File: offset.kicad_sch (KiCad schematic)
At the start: 37 parts, among them U11 OPA2189DGK, U12 TMUX1108PW, U18 DG419D, U19 TCA0372

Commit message: Tweaks following spice simulation.
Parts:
- removed R120, R121: 0R33, Resistor_SMD:R_0805_2012Metric, symbol Device:R
- C101, C102: value 1u -> 10n; footprint Capacitor_SMD:C_0402_1005Metric -> Capacitor_SMD:C_0603_1608Metric; LCSC C52923 -> C307500
- C104, C116: value 0u1 -> 1u; LCSC C307331 -> C52923
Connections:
- net at C110.1, C112.1, U19.1 (VCC): now also L11.2
- net at L12.2: now also C111.2, C113.2, U19.12 (VEE), U19.13 (VEE), U19.4 (VEE), U19.5 (VEE)
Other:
- moved on the sheet: C110, C111, C112, C113, C116, L11, L12, U18, U19C

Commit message: About to delete scan...
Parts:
- R114, R116: Stock (none) -> 50
- U11: Stock (none) -> 15
- U12, U19: Stock (none) -> 3
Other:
- note added: "FIXME - can drive capacitance via mux?"

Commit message: Scan deleted.
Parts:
- removed C110, C111: 10u, Capacitor_SMD:C_0805_2012Metric, symbol Device:C
- removed C112, C113, C114, C115: 0u1, Capacitor_SMD:C_0402_1005Metric, symbol Device:C
- removed C116: 1u, Capacitor_SMD:C_0402_1005Metric, symbol Device:C
- removed L11, L12: 100, Inductor_SMD:L_0603_1608Metric, symbol Parts:L_Ferrite_Power
- removed U18: DG419D, Package_SO:SOIC-8_3.9x4.9mm_P1.27mm, symbol Parts:DG419
- removed U19: TCA0372, Package_SO:SOIC-16W_7.5x10.3mm_P1.27mm, symbol Parts:TCA0372

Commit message: Most blocks there....
About to restore scan.
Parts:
- added R119: 100, Resistor_SMD:R_0402_1005Metric, symbol Device:R
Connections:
- net 5V: now also R119.2; no longer R101.1, U11.1, U11.2 (-)
- new net: R101.1, R119.1, U11.1, U11.2 (-)
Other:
- note removed: "FIXME - can drive capacitance via mux?"
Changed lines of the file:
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@@
 		(title "Offset Voltage Generation")
 	)
-	(text "FIXME - can drive capacitance via mux?\n"
-		(exclude_from_sim no)
-		(at 143.256 56.134 0)
-		(effects
-			(font
-				(size 1.27 1.27)
-			)
-		)
-	)
 	(text_box "Tie the ladder grounds together with the compensation resistances to cancel currents."
 		(exclude_from_sim no)
@@
 	(wire
 		(pts
-			(xy 123.19 59.69) (xy 143.51 59.69)
+			(xy 123.19 59.69) (xy 124.46 59.69)
 		)
 		(stroke
@@
 	(wire
 		(pts
+			(xy 132.08 59.69) (xy 143.51 59.69)
+		)
+		(stroke
+			(width 0)
+			(type default)
+		)
+	)
+	(wire
+		(pts
 			(xy 95.25 57.15) (xy 100.33 57.15)
 		)
@@
 		(dnp no)
 		(property "Reference" "R101"
-			(at 130.81 61.214 90)
+			(at 125.73 63.246 90)
 			(effects
 				(font
 					(size 1.27 1.27)
 				)
-				(justify right)
+				(justify left)
 			)
 		)
@@
 		(dnp no)
 		(property "Reference" "R102"
-			(at 125.476 65.024 90)
+			(at 130.81 67.056 90)
 			(effects
 				(font
 					(size 1.27 1.27)
 				)
-				(justify left)
+				(justify right)
 			)
 		)
@@
 					(unit 1)
 				)
+			)
+		)
+	)
+	(symbol
+		(lib_id "Device:R")
+		(at 128.27 59.69 90)
+		(unit 1)
+		(exclude_from_sim no)
+		(in_bom yes)
+		(on_board yes)
+		(dnp no)
+		(property "Reference" "R119"
+			(at 128.27 57.658 90)
+			(effects
+				(font
+					(size 1.27 1.27)
+				)
+			)
+		)
+		(property "Value" "100"
+			(at 128.27 59.69 90)
+			(effects
+				(font
+					(size 1.27 1.27)
+				)
+			)
+		)
+		(property "Footprint" "Resistor_SMD:R_0402_1005Metric"
+			(at 128.27 61.468 90)
+			(effects
+				(font
+					(size 1.27 1.27)
+				)
+				(hide yes)
+			)
+		)
+		(property "Datasheet" "~"
+			(at 128.27 59.69 0)
+			(effects
+				(font
+					(size 1.27 1.27)
+				)
+				(hide yes)
+			)
+		)
+		(property "Description" "Resistor"
+			(at 128.27 59.69 0)
+			(effects
+				(font
+					(size 1.27 1.27)
+				)
+				(hide yes)
+			)
+		)
+		(property "LCSC" "C25076"
+			(at 128.27 59.69 90)
+			(effects
+				(font
+					(size 1.27 1.27)
+				)
+				(hide yes)
+			)
+		)
+		(property "Stock" ""
+			(at 128.27 59.69 90)
+			(effects
+				(font
+					(size 1.27 1.27)
+				)
+				(hide yes)
+			)
+		)
+		(pin "1"
+		)
+		(pin "2"
+		)
+		(instances
+			(project "lincal"
+				(path "/b054cef4-39e3-49d8-aff0-7ba5a206c187/fd210975-34eb-456f-9075-cf344b0a559b"
+					(reference "R119")
+					(unit 1)
+				)

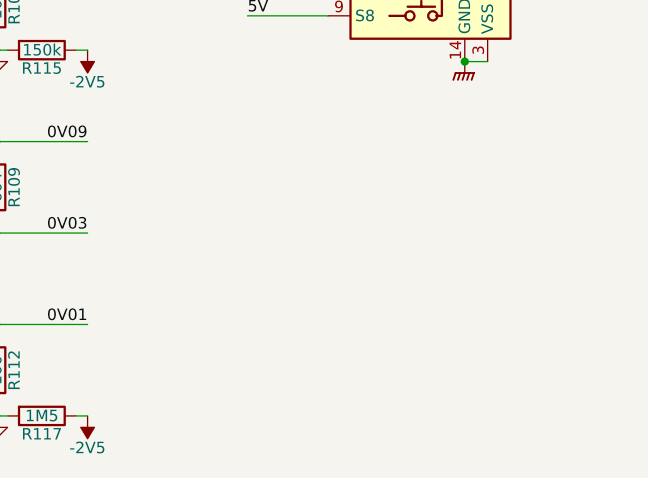
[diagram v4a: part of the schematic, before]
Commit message: S&H restored.  Now to touch up connections etc.
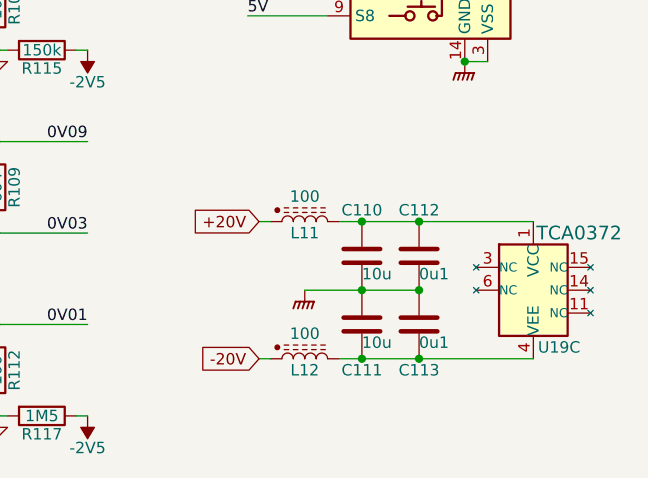
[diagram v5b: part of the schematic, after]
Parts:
- added C110, C111: 10u, Capacitor_SMD:C_0805_2012Metric, symbol Device:C
- added C112, C113: 0u1, Capacitor_SMD:C_0402_1005Metric, symbol Device:C
- added L11, L12: 100, Inductor_SMD:L_0603_1608Metric, symbol Parts:L_Ferrite_Power
- added U19: TCA0372, Package_SO:SOIC-16W_7.5x10.3mm_P1.27mm, symbol Parts:TCA0372
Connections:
- net GNDPWR: now also C110.2, C111.1, C112.2, C113.1
- new net: C110.1, C112.1, L11.2, U19.1 (VCC)
- new net: C111.2, C113.2, L12.2, U19.12 (VEE), U19.13 (VEE), U19.4 (VEE), U19.5 (VEE)
- new net +20V: L11.1
- new net -20V: L12.1

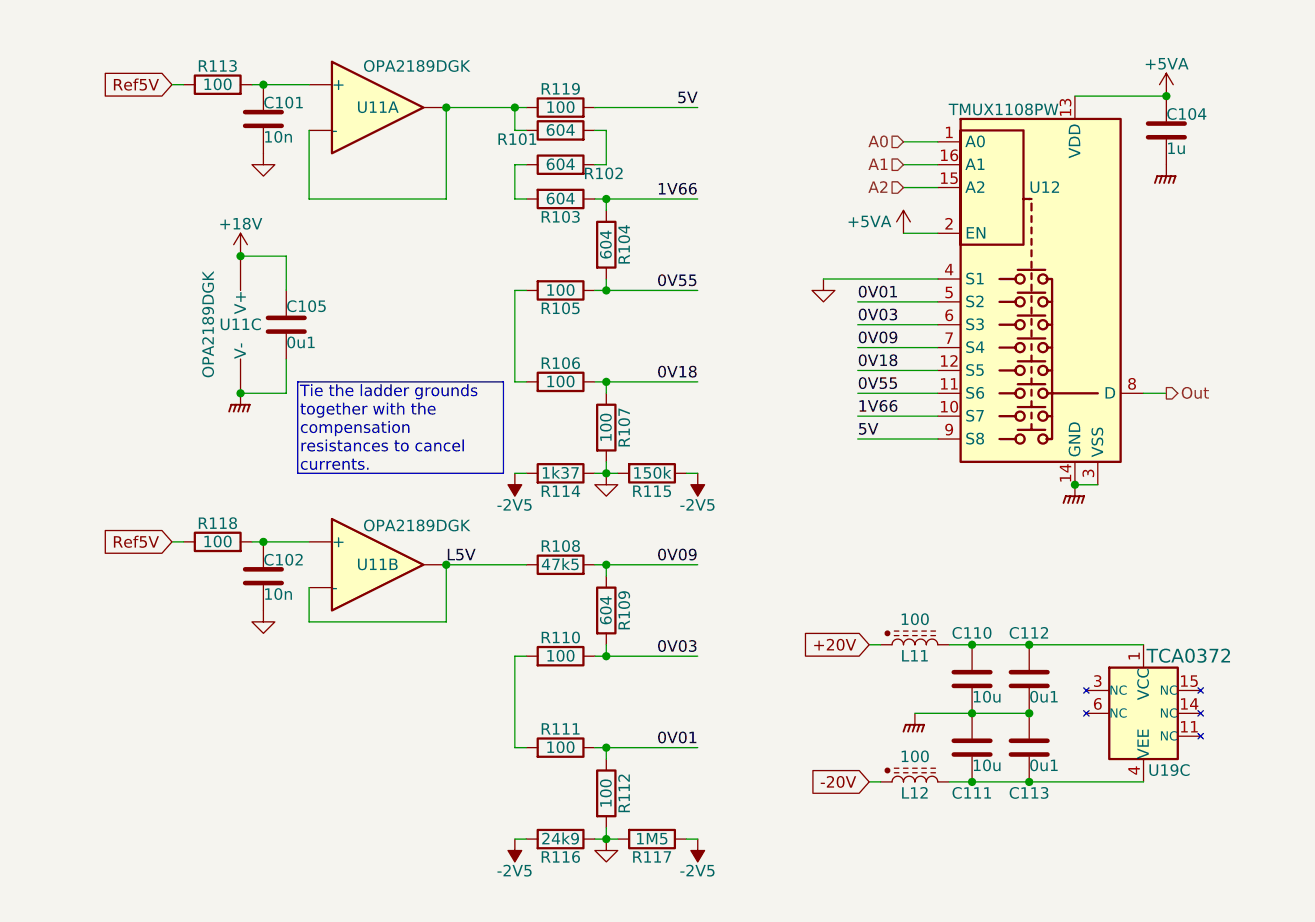
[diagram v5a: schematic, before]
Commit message: Put ref filtering into the schematic.
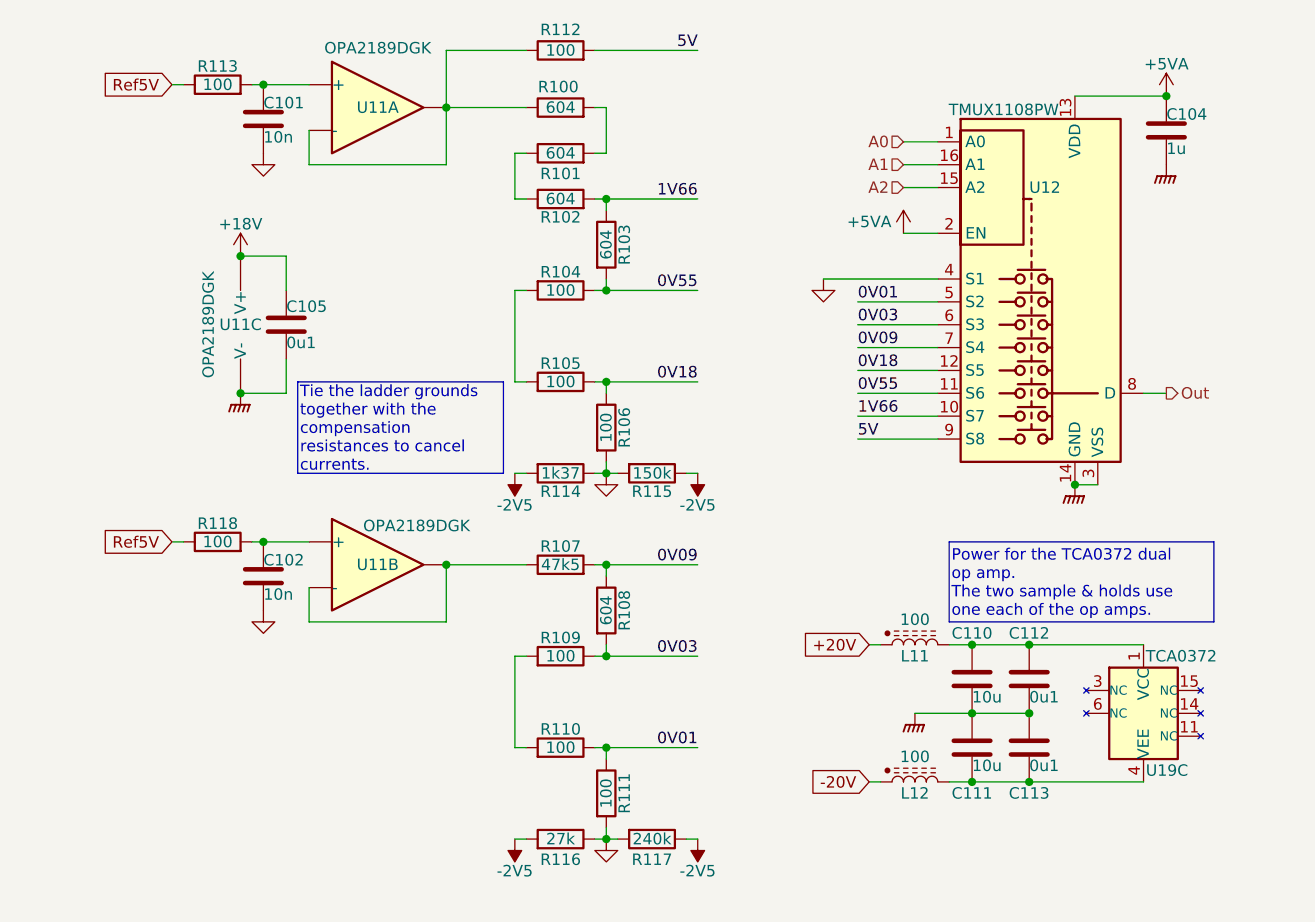
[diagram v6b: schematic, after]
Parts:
- removed R103: 604, Resistor_SMD:R_0603_1608Metric, symbol Device:R
- removed R119: 100, Resistor_SMD:R_0402_1005Metric, symbol Device:R
- added R100: 604, Resistor_SMD:R_0805_2012Metric, symbol Device:R
- added R112: 100, Resistor_SMD:R_0402_1005Metric, symbol Device:R
- R101, R102: footprint Resistor_SMD:R_0603_1608Metric -> Resistor_SMD:R_0805_2012Metric
- R114: footprint Resistor_SMD:R_0603_1608Metric -> (none); Stock 50 -> (none)
- R116: value 24k9 -> 27k; Stock 50 -> (none); now in the parts list
- R117: value 1M5 -> 240k; LCSC C4172 -> (none)
- renumbered R104 to R103, R105 to R104, R106 to R105, R107 to R106, R108 to R107, R109 to R108, R110 to R109, R111 to R110, R112 to R111
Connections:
- net 1V66: now also R102.2
- net 5V: now also R112.2
- net at U11.1, U11.2 (-): now also R100.1, R112.1; no longer R101.1
- net at R101.2: now also R100.2; no longer R102.2
- net at R102.1: now also R101.1
- net L5V: no longer names the net of R107.1, U11.6 (-), U11.7
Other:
- moved on the sheet: R101, R102

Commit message: Adjust voltage rails.
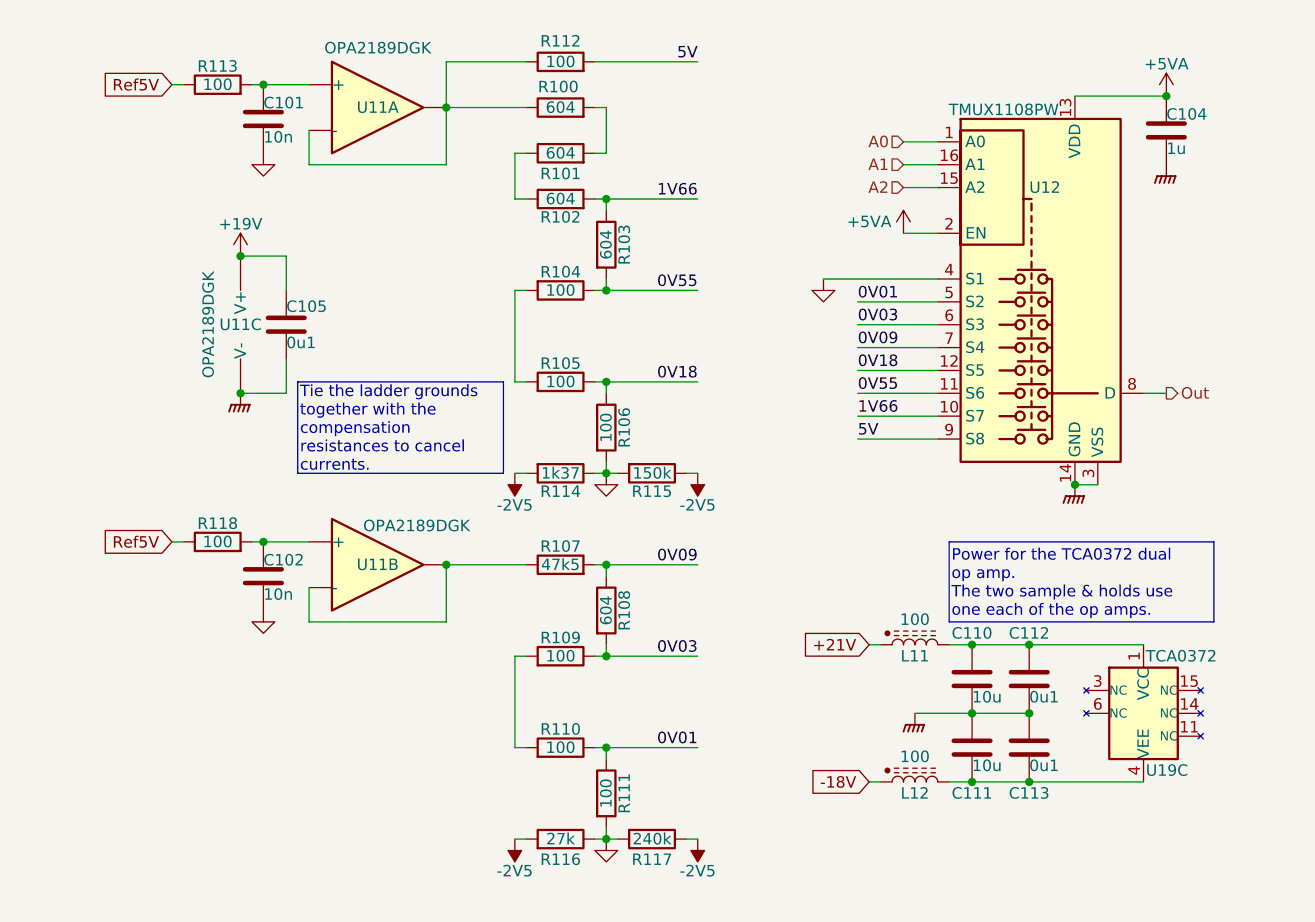
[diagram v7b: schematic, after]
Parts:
- R100, R101, R102: footprint Resistor_SMD:R_0805_2012Metric -> Resistor_SMD:R_0603_1608Metric
- R114: footprint (none) -> Resistor_SMD:R_0603_1608Metric; Stock (none) -> 50
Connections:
- net +18V renamed +19V
- net +20V renamed +21V
- net -20V renamed -18V
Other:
- moved on the sheet: R112
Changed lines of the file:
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@@
 	(wire
 		(pts
-			(xy 124.46 53.34) (xy 115.57 53.34)
+			(xy 124.46 54.61) (xy 115.57 54.61)
 		)
 		(stroke
@@
 	(wire
 		(pts
-			(xy 132.08 53.34) (xy 143.51 53.34)
+			(xy 132.08 54.61) (xy 143.51 54.61)
 		)
 		(stroke
@@
 	(wire
 		(pts
-			(xy 115.57 53.34) (xy 115.57 59.69)
+			(xy 115.57 54.61) (xy 115.57 59.69)
 		)
 		(stroke
@@
 	)
 	(label "5V"
-		(at 143.51 53.34 180)
+		(at 143.51 54.61 180)
 		(effects
 			(font
@@
 		)
 	)
-	(global_label "+20V"
+	(global_label "+21V"
 		(shape input)
 		(at 162.56 119.38 180)
@@
 		)
 	)
-	(global_label "-20V"
+	(global_label "-18V"
 		(shape input)
 		(at 162.56 134.62 180)
@@
 			)
 		)
-		(property "Footprint" "Resistor_SMD:R_0805_2012Metric"
+		(property "Footprint" "Resistor_SMD:R_0603_1608Metric"
 			(at 128.27 66.548 90)
 			(effects
@@
 	)
 	(symbol
-		(lib_id "Parts:+18V")
+		(lib_id "Parts:+19V")
 		(at 92.71 76.2 0)
 		(mirror y)
@@
 		(on_board yes)
 		(dnp no)
-		(property "Reference" "#PWR0117"
+		(property "Reference" "#PWR117"
 			(at 92.71 80.01 0)
 			(effects
@@
 			)
 		)
-		(property "Value" "+18V"
+		(property "Value" "+19V"
 			(at 92.71 72.644 0)
 			(do_not_autoplace yes)
@@
 			)
 		)
-		(property "Description" "Power symbol creates a global label with name {dblquote}+18V{dblquote}"
+		(property "Description" "Power symbol creates a global label with name \"+19\""
 			(at 92.71 76.2 0)
 			(effects
@@
 			(project ""
 				(path "/b054cef4-39e3-49d8-aff0-7ba5a206c187/fd210975-34eb-456f-9075-cf344b0a559b"
-					(reference "#PWR0117")
+					(reference "#PWR117")
 					(unit 1)
 				)
@@
 	(symbol
 		(lib_id "Device:R")
-		(at 128.27 53.34 90)
+		(at 128.27 54.61 90)
 		(unit 1)
 		(exclude_from_sim no)
@@
 		(dnp no)
 		(property "Reference" "R112"
-			(at 128.27 51.054 90)
+			(at 128.27 52.324 90)
 			(effects
 				(font
@@
 		)
 		(property "Value" "100"
-			(at 128.27 53.34 90)
+			(at 128.27 54.61 90)
 			(effects
 				(font
@@
 		)
 		(property "Footprint" "Resistor_SMD:R_0402_1005Metric"
-			(at 128.27 55.118 90)
+			(at 128.27 56.388 90)
 			(effects
 				(font
@@
 		)
 		(property "Datasheet" "~"
-			(at 128.27 53.34 0)
+			(at 128.27 54.61 0)
 			(effects
 				(font
@@
 		)
 		(property "Description" "Resistor"
-			(at 128.27 53.34 0)
+			(at 128.27 54.61 0)
 			(effects
 				(font
@@
 		)
 		(property "LCSC" "C25076"
-			(at 128.27 53.34 90)
+			(at 128.27 54.61 90)
 			(effects
 				(font
@@
 		)
 		(property "Stock" ""
-			(at 128.27 53.34 90)
+			(at 128.27 54.61 90)
 			(effects
 				(font
@@
 			)
 		)
-		(property "Footprint" ""
+		(property "Footprint" "Resistor_SMD:R_0603_1608Metric"
 			(at 128.27 98.552 90)
 			(effects
@@
 			)
 		)
-		(property "Stock" ""
+		(property "Stock" "50"
 			(at 128.27 100.33 90)
 			(effects
@@
 			)
 		)
-		(property "Footprint" "Resistor_SMD:R_0805_2012Metric"
+		(property "Footprint" "Resistor_SMD:R_0603_1608Metric"
 			(at 128.27 61.468 90)
 			(effects
@@
 			)
 		)
-		(property "Footprint" "Resistor_SMD:R_0805_2012Metric"
+		(property "Footprint" "Resistor_SMD:R_0603_1608Metric"
 			(at 128.27 71.628 90)
 			(effects

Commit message: Progress checkin.  About to redo FDA feedback again.
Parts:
- removed C110, C111: 10u, Capacitor_SMD:C_0805_2012Metric, symbol Device:C
- removed C112, C113: 0u1, Capacitor_SMD:C_0402_1005Metric, symbol Device:C
- removed L11, L12: 100, Inductor_SMD:L_0603_1608Metric, symbol Parts:L_Ferrite_Power
- removed U19: TCA0372, Package_SO:SOIC-16W_7.5x10.3mm_P1.27mm, symbol Parts:TCA0372
